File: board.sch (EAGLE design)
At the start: 5 parts, among them M1 ARDUINO-NANO-3.0#ISP

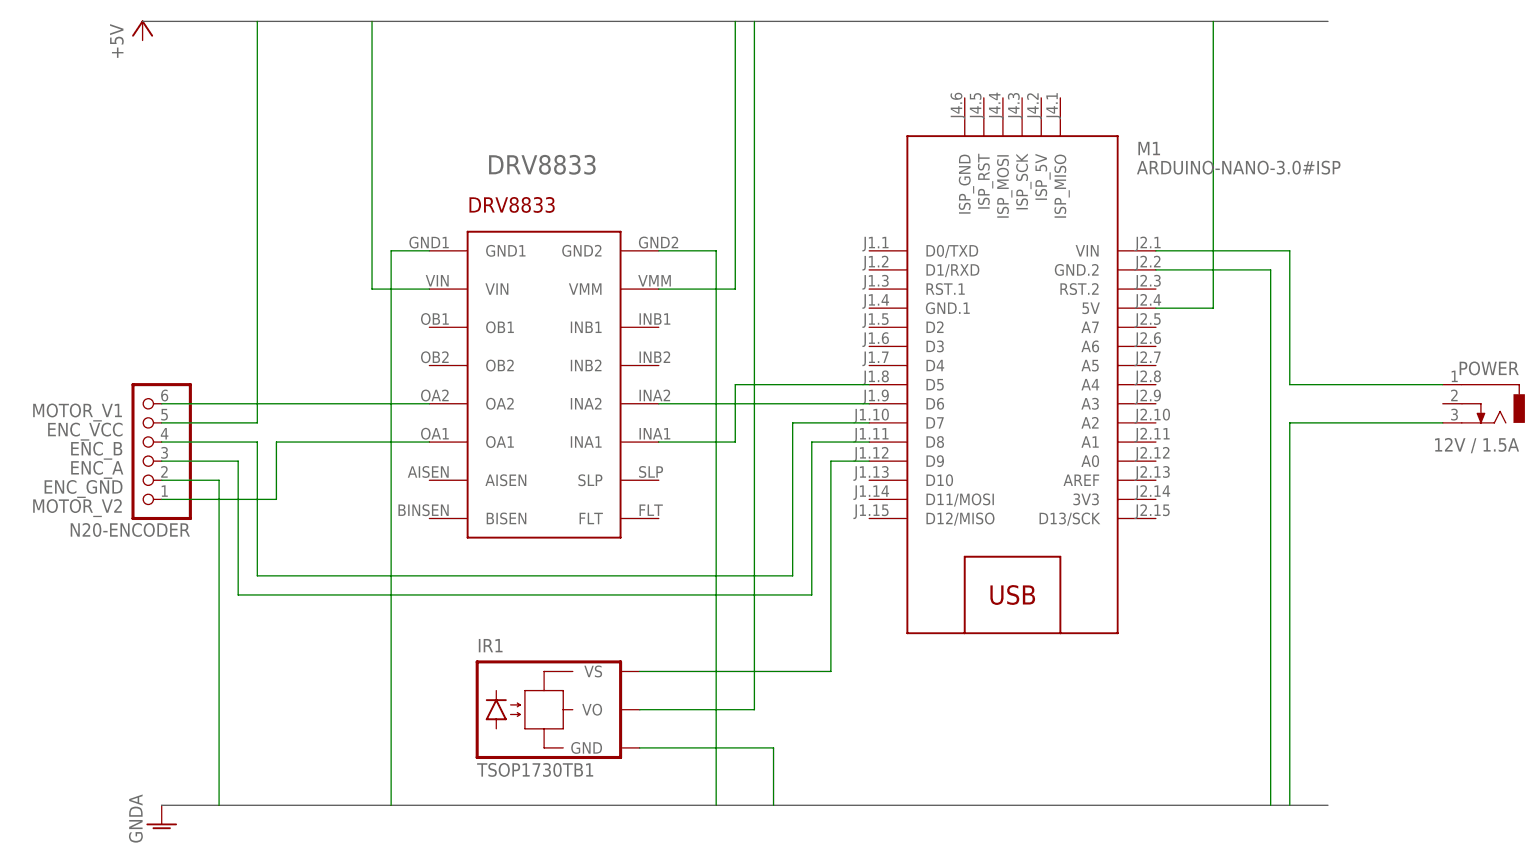
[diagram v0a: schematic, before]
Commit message: [IMPROVEMENT] remove bus and added regular net with junctions
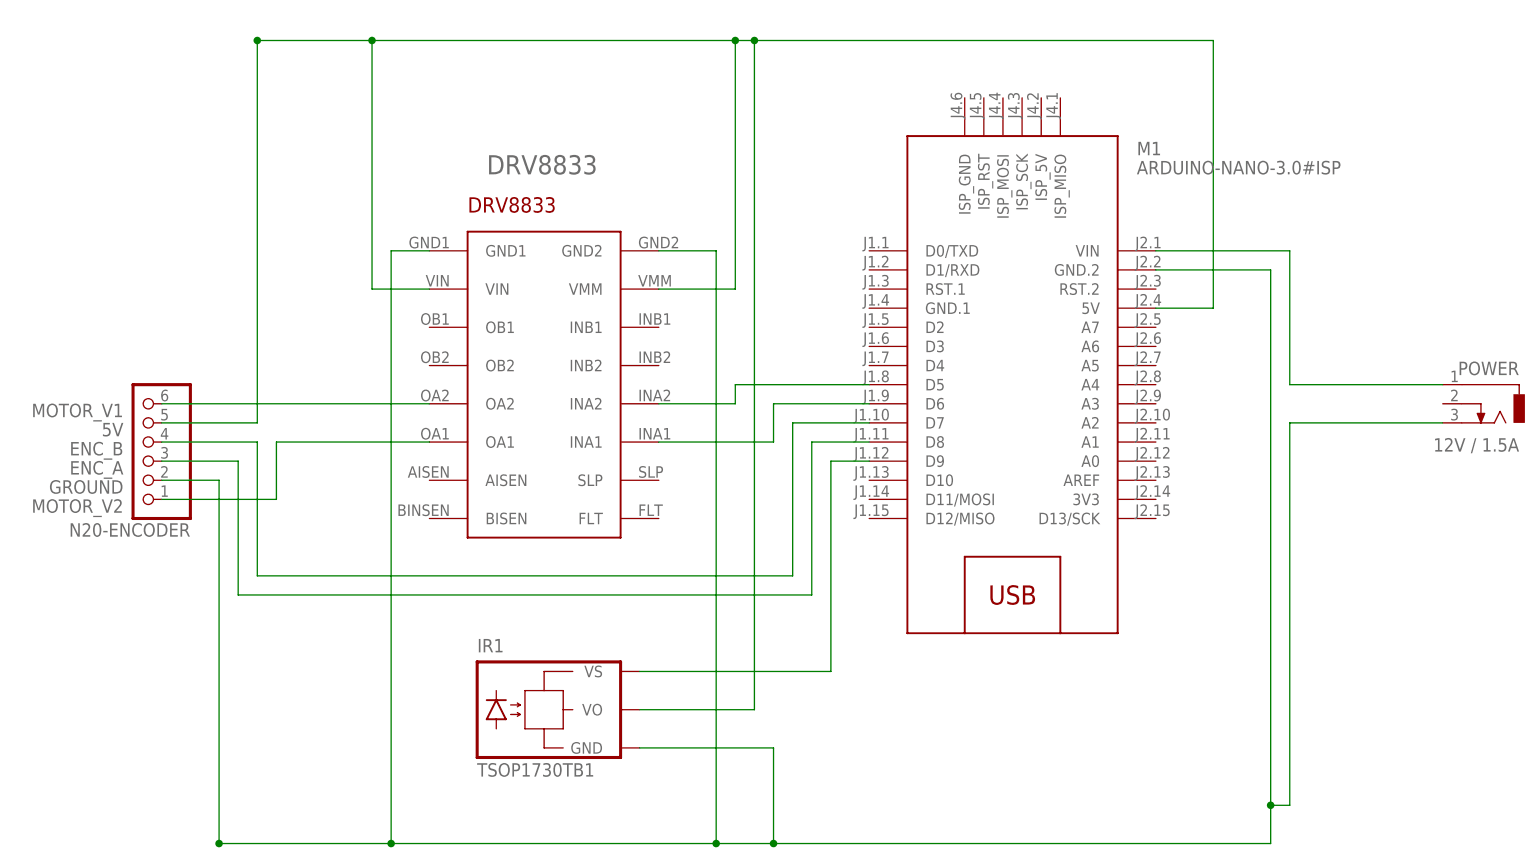
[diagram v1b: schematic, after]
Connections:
- removed net ARDUINO_GROUND: M1.GND.2
- removed net ARDUINO_VOLTAGE: M1.5V
- removed net DRIVER_GROUND: DRV8833.GND1, DRV8833.GND2
- removed net DRIVER_VOLTAGE_CONTROL: DRV8833.VIN
- removed net DRIVER_VOLTAGE_MOTOR: DRV8833.VMM
- removed net ENC_GND: N20-ENCODER.2
- removed net ENC_VCC: N20-ENCODER.5
- removed net IR_GROUND: IR1.GND
- removed net IR_VOLTAGE: IR1.VO
- removed net MOTOR_CONTROL_2: DRV8833.INA2, M1.D6
- removed net POWER_GND: POWER.3
- new net 5V: DRV8833.VIN, DRV8833.VMM, IR1.VO, M1.5V, N20-ENCODER.5
- new net GROUND: DRV8833.GND1, DRV8833.GND2, IR1.GND, M1.GND.2, N20-ENCODER.2, POWER.3
- new net N$1: DRV8833.INA1, M1.D6
- net MOTOR_CONTROL_1: now also DRV8833.INA2; no longer DRV8833.INA1
